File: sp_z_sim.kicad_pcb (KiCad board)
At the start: 2 copper layers, 106 parts, among them J1 USB_B_Micro, J10 ADC_EXTRA, J11 IN+, J12 IN-, J2 TEMP1, J3 TEMP1, J4 SWD, J5 Micro_SD_Card_Det, J6 OUT1, J7 OUT2, J8 4T_1, J9 4T_2, Q1 Q_NMOS_GSD, Q2 Q_NMOS_GSD, Q3 Q_NMOS_GSD, Q4 Q_NMOS_GSD, Q5 Q_NMOS_GSD, U1 OPA549, U10 AZ1117-3.3, U2 INA240A1D, U3 OPA549, U4 INA240A1D, U5 PDS760-13, U6 TPS54561DPRR, U7 STM32F405RGTx, U8 ADR4533BRZ, U9 TPS54160, Y1 Crystal_GND24

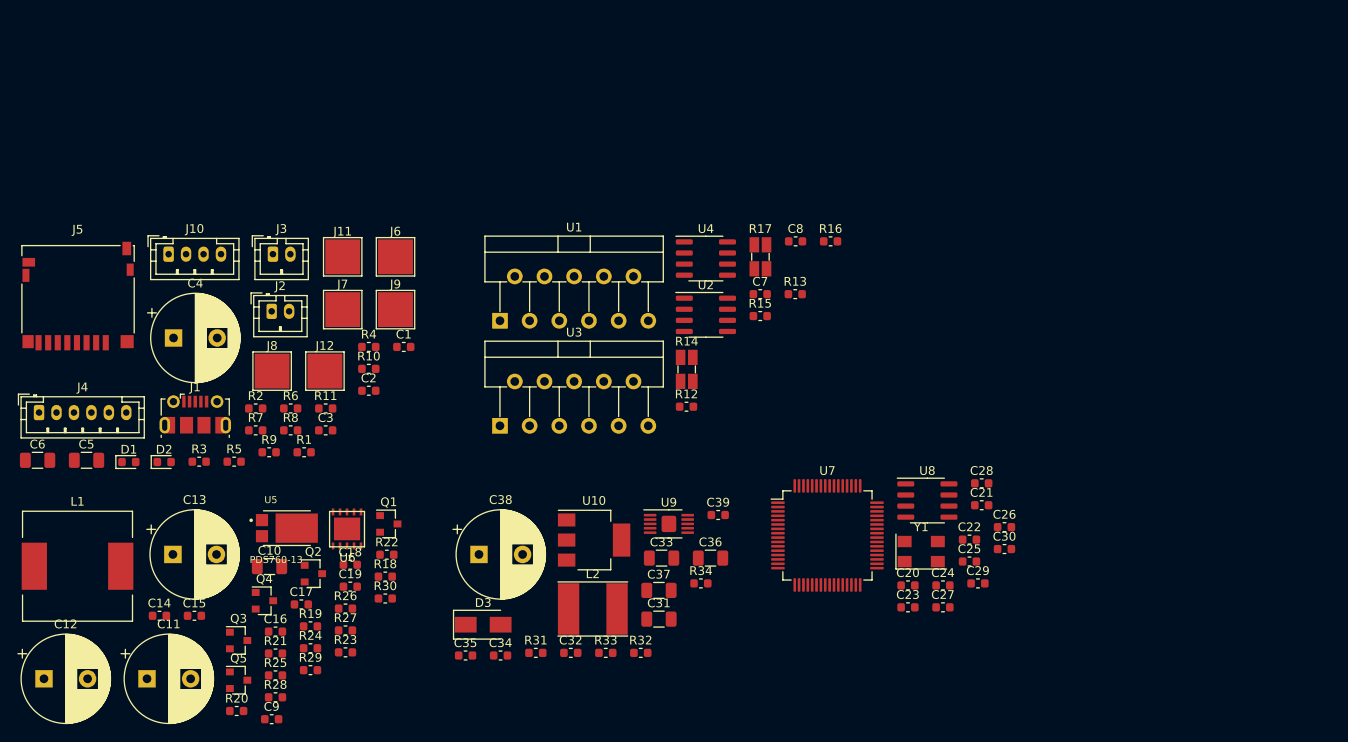
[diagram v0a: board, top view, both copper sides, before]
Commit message: preparation for routing and adding kylfläns
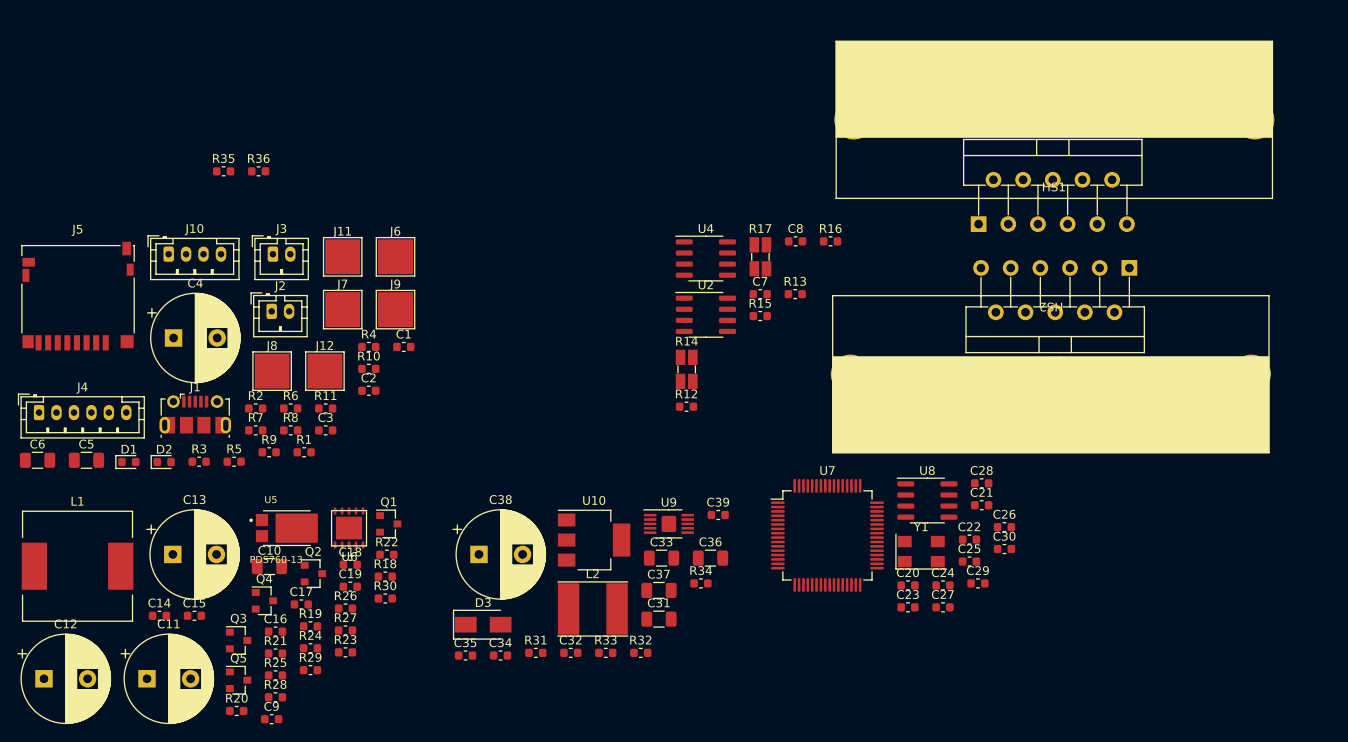
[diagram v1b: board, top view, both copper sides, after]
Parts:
- added HS1: OMNI-220-18-50-2C, rise_elp:OMNI-220-18-50-2C, F.Cu at (223.3, 56.5)
- added HS2: OMNI-220-18-50-2C, rise_elp:OMNI-220-18-50-2C, F.Cu at (222.9, 85.7)
- added R35: 22R, Resistor_SMD:R_0603_1608Metric, F.Cu at (128.1, 62.4)
- added R36: 22R, Resistor_SMD:R_0603_1608Metric, F.Cu at (132.1, 62.4)
- moved U1 72.4 mm to (231.9, 73.5), turned to 180 degrees
- moved U3 59.5 mm to (214.7, 68.5)
- moved U6 0.25 mm to (142.5, 103.3)
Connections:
- J1 pad 2: /USB_DM -> Net-(J1-Pad2)
- J1 pad 3: /USB_DP -> Net-(J1-Pad3)

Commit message: Schematic updates, added 3D models and started routing
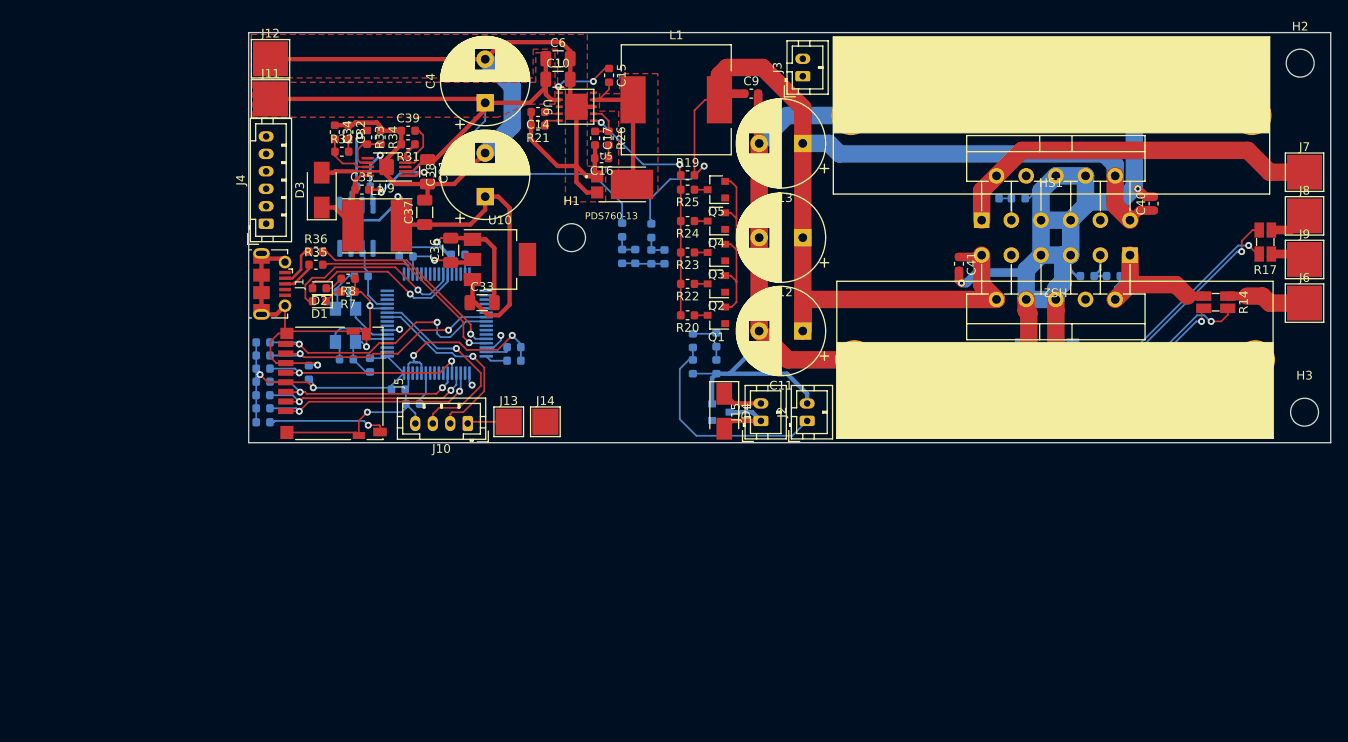
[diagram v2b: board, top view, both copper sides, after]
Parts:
- removed C28: 2.2u, Capacitor_SMD:C_0603_1608Metric
- removed C5: 2.2u, Capacitor_SMD:C_1206_3216Metric
- added C40: 2.2u, Capacitor_SMD:C_0603_1608Metric, F.Cu at (234.7, 66.1)
- added C41: 2.2u, Capacitor_SMD:C_0603_1608Metric, F.Cu at (212.4, 73.0)
- added D4: SCH, Diode_SMD:D_SMA, F.Cu at (185.5, 89.9)
- added H1: MountingHole, MountingHole:MountingHole_3.2mm_M3, F.Cu at (168.0, 70.0)
- added H2: MountingHole, MountingHole:MountingHole_3.2mm_M3, F.Cu at (251.5, 50.0)
- added H3: MountingHole, MountingHole:MountingHole_3.2mm_M3, F.Cu at (252.0, 90.0)
- added J13: CAL_3.3, TestPoint:TestPoint_Pad_3.0x3.0mm, F.Cu at (160.8, 91.1)
- added J14: CAL_3.3, TestPoint:TestPoint_Pad_3.0x3.0mm, F.Cu at (165.0, 91.1)
- added J15: FAN, Connector_JST:JST_PH_B2B-PH-K_1x02_P2.00mm_Vertical, F.Cu at (189.7, 91.0)
- added Q6: Q_NMOS_GSD, Package_TO_SOT_SMD:SOT-23, B.Cu at (185.1, 90.0)
- C1, C18, C19, C2, C20, C21, C22, C23, C24, C25, C26, C27, C29, C3, C30, C7, C8, R1, R10, R11, R12, R13, R15, R16, R18, R2, R27, R28, R29, R3, R30, R4, R5, R6, R9, U7, U8, Y1: moved to B.Cu
- HS1, HS2: value OMNI-220-18-50-2C -> Heatsink_Pad
- R14, R17: value R_Shunt -> r_shunt_lvk
- U2, U4: value INA240A1D -> INA240A1PW; footprint Package_SO:SOIC-8_3.9x4.9mm_P1.27mm -> Package_SO:TSSOP-8_4.4x3mm_P0.65mm; moved to B.Cu
- moved J8 119.6 mm to (252.0, 67.5)
- moved J7 111.3 mm to (252.0, 62.5)
- moved J9 104.3 mm to (252.0, 72.5)
- moved J6 104.3 mm to (252.0, 77.5)
- moved C12 100.6 mm to (194.5, 70.0), turned to 180 degrees
- moved C9 90.3 mm to (188.6, 53.5)
- moved L1 87.0 mm to (180.0, 54.2)
- moved C13 86.2 mm to (194.5, 59.2), turned to 180 degrees
- moved C11 85.1 mm to (194.5, 80.7), turned to 180 degrees
- moved C30 84.4 mm to (144.2, 64.2), turned to 180 degrees
- moved C29 79.0 mm to (143.9, 74.4)
- moved Q5 78.5 mm to (184.6, 64.5), turned to 180 degrees
- moved C15 78.1 mm to (172.3, 51.4), turned to -90 degrees
- moved C21 77.0 mm to (141.9, 76.2)
- moved C6 75.3 mm to (166.4, 49.5)
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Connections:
- net /ENABLE renamed /PB7_OUT_EN
- net /PB4_VSEL_3 renamed /VSEL3
- net /PWR_DIV renamed /PA3_DCDC_IN
- net /VSEL4 renamed /PB5_VSEL_4
- net /VSEL5 renamed /PB6_VSEL_5
- HS1 pad 1: (no net) -> GND
- HS2 pad 1: (no net) -> GND
- R12 pad 1: Net-(R5-Pad1) -> Net-(R12-Pad1)
- R14 pad 2: Net-(R7-Pad2) -> Net-(R14-Pad2)
- R14 pad 3: Net-(R7-Pad3) -> Net-(R12-Pad1)
- R14 pad 4: Net-(R5-Pad1) -> Net-(R14-Pad4)
- R17 pad 2: Net-(R10-Pad2) -> Net-(R17-Pad2)
- R17 pad 3: Net-(R10-Pad3) -> /SENSE_4T_1
- R17 pad 4: /SENSE_4T_1 -> Net-(R17-Pad4)
- U1 pad 1: Net-(R5-Pad1) -> Net-(R12-Pad1)
- U1 pad 2: Net-(R5-Pad1) -> Net-(R12-Pad1)
- U2 pad 1: Net-(R7-Pad3) -> GND
- U2 pad 2: GND -> Net-(R14-Pad2)
- U2 pad 3: +3.3VA -> Net-(R14-Pad4)
- U2 pad 5: /PA0_SHUNT1 -> +3.3VA
- U2 pad 8: Net-(R7-Pad2) -> /PA0_SHUNT1
- U4 pad 1: Net-(R10-Pad3) -> GND
- U4 pad 2: GND -> Net-(R17-Pad2)
- U4 pad 3: +3.3VA -> Net-(R17-Pad4)
- U4 pad 5: /PA1_SHUNT2 -> +3.3VA
- U4 pad 8: Net-(R10-Pad2) -> /PA1_SHUNT2
- U7 pad 61: Net-(U7-Pad61) -> /PB8_FAN
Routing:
- net GND: track 0.00 -> 628.6 mm, vias 0 -> 11
- net OUT_RAIL: track 0.00 -> 147.4 mm, vias 0 -> 1
- net PWR_IN: track 0.00 -> 81.7 mm
- net +5V: track 0.00 -> 60.9 mm, vias 0 -> 2
- net /SWDIO: track 0.00 -> 53.6 mm, vias 0 -> 1
- net /OUT2: track 0.00 -> 46.4 mm
- net +3V3: track 0.00 -> 46.3 mm, vias 0 -> 3
- net /SWCLK: track 0.00 -> 39.3 mm, vias 0 -> 1
- net +3.3VA: track 0.00 -> 32.0 mm, vias 0 -> 2
- net /SDIO_D1: track 0.00 -> 30.5 mm, vias 0 -> 2
- net /DCDC/FB: track 0.00 -> 29.3 mm, vias 0 -> 2
- net /SDIO_D0: track 0.00 -> 28.6 mm, vias 0 -> 2
- net Net-(R17-Pad4): track 0.00 -> 27.8 mm, vias 0 -> 1
- net Net-(R17-Pad2): track 0.00 -> 26.7 mm, vias 0 -> 1
- net /SDIO_D2: track 0.00 -> 26.5 mm, vias 0 -> 2
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- added copper zone on F.Cu, net /DCDC/SW
- added copper zone on F.Cu, net GND
- added copper zone on F.Cu, net PWR_IN
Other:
- board outline added: 124 x 47 mm
- copper layers 2 -> 4
- rule via_min_size: 0.4 -> 0.6

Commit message: Some routing updates
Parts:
- moved J15 0.70 mm to (189.0, 91.0)
- moved D4 0.50 mm to (185.0, 89.9)
- moved H1 0.50 mm to (167.5, 70.0)
- moved H3 0.50 mm to (251.5, 90.0)
- moved J2 0.50 mm to (194.5, 91.0)
- moved HS2 0.40 mm to (223.0, 84.0)
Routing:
- net Net-(D4-Pad2): track 8.59 -> 7.69 mm
- net GND: track 628.6 -> 628.0 mm

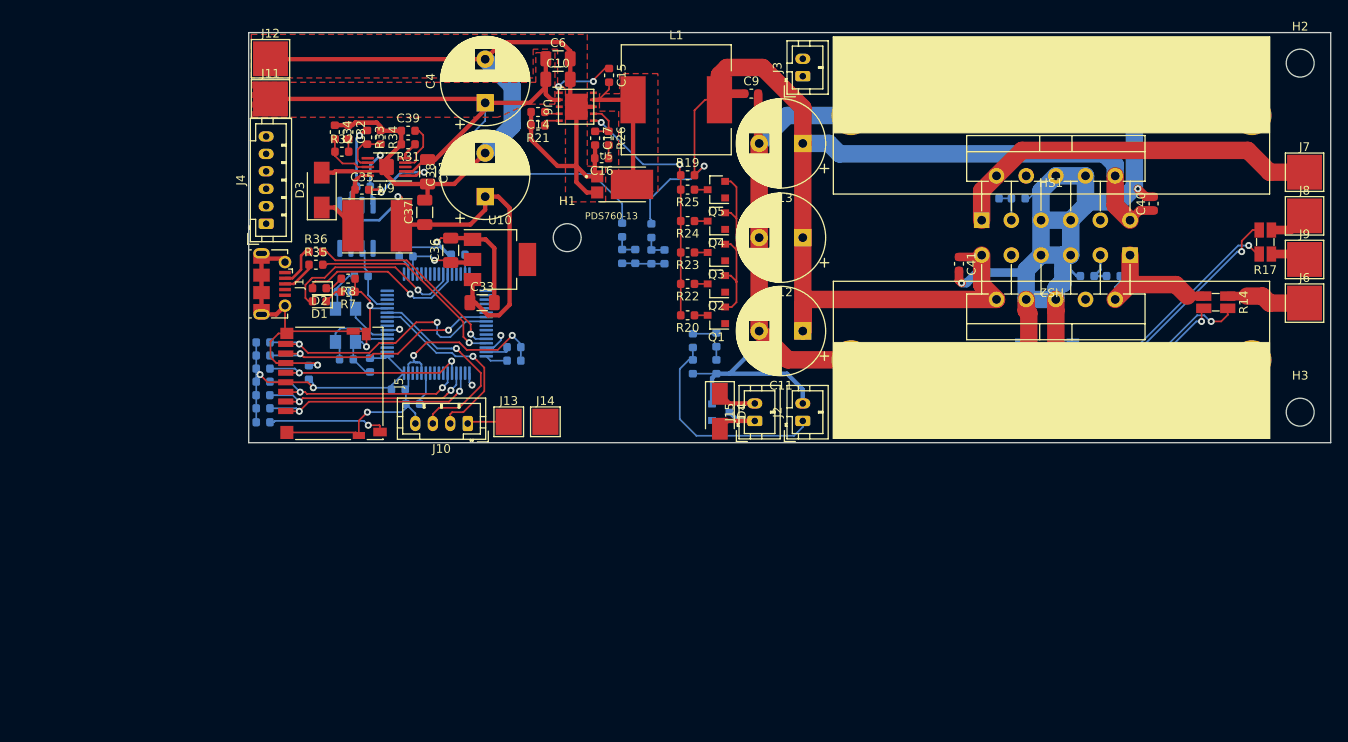
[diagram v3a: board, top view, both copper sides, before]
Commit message: Finished routing and added some 3D models
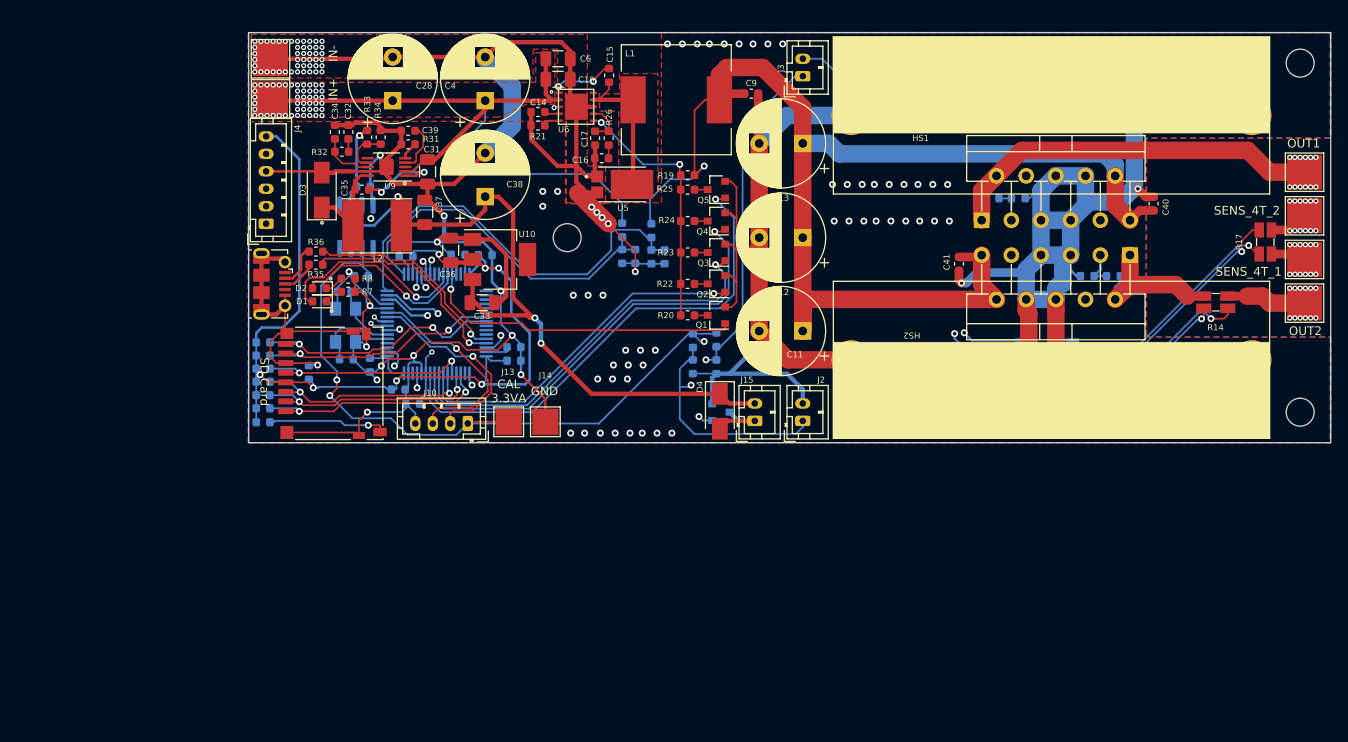
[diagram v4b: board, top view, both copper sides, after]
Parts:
- added C28: 100u, Capacitor_THT:CP_Radial_D10.0mm_P5.00mm, F.Cu at (147.5, 54.3)
- added C5: 2.2u, Capacitor_SMD:C_0603_1608Metric, B.Cu at (158.1, 72.0)
- moved C4 0.25 mm to (158.1, 54.3)
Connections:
- net /VSEL3 renamed /PB4_VSEL_3
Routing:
- net +3.3VA: track 32.0 -> 143.7 mm, vias 2 -> 5
- net /PA7_ES2: track 0.00 -> 104.0 mm, vias 0 -> 1
- net GND: track 628.0 -> 728.3 mm, vias 11 -> 166
- net /PA4_DAC1: track 0.00 -> 85.3 mm, vias 0 -> 1
- net /PC1_TEMP2: track 1.53 -> 84.8 mm, vias 0 -> 2
- net /PA6_ES1: track 0.00 -> 81.0 mm, vias 0 -> 1
- net /PA5_DAC2: track 0.00 -> 79.3 mm, vias 0 -> 1
- net /PA0_SHUNT1: track 0.00 -> 79.0 mm, vias 0 -> 2
- net /PA1_SHUNT2: track 0.00 -> 76.3 mm, vias 0 -> 2
- net +3V3: track 46.3 -> 119.2 mm, vias 3 -> 7
- net /PB6_VSEL_5: track 0.00 -> 57.1 mm, vias 0 -> 1
- net /PB5_VSEL_4: track 0.00 -> 51.7 mm, vias 0 -> 1
- net /PB4_VSEL_3: track 0.00 -> 46.3 mm, vias 0 -> 1
- net /PA2_DCDC_RAIL: track 2.92 -> 48.1 mm
- net /PC0_TEMP1: track 25.1 -> 70.1 mm, vias 0 -> 2
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- added copper zone on B.Cu, net GND
- added copper zone on In1.Cu, net GND
- added copper zone on In2.Cu, net GND
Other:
- board text added: "3.3VA"
- board text added: "5V"
- board text added: "CAL 3.3VA"
- board text added: "FAN"
- board text added: "GND"
- board text added: "IN+"
- board text added: "IN-"
- board text added: "NC"
- board text added: "NRST"
- board text added: "OUT1"
- board text added: "OUT2"
- board text added: "PC2"
- board text added: "PC3"
- board text added: "SD Card"
- board text added: "SENS_4T_1"
- board text added: "SENS_4T_2"
- board text added: "SWCLK"
- board text added: "SWDIO"
- board text added: "TEMP1"
- board text added: "TEMP2"
- board text added: "VCC"
